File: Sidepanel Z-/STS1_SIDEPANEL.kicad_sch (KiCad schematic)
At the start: 7 parts, among them J1 Conn_01x18, J3 Conn_01x12

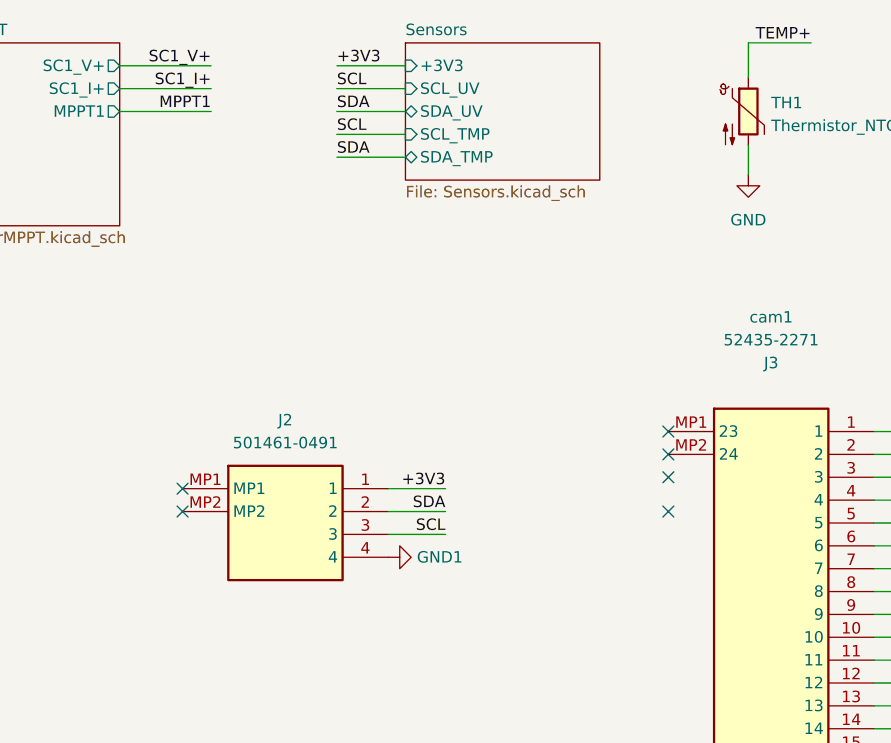
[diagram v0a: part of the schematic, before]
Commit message: replace ZF5S-*-01-T-WT and 2005280040 connectors with T1M-*-F-SH-L-FR connector
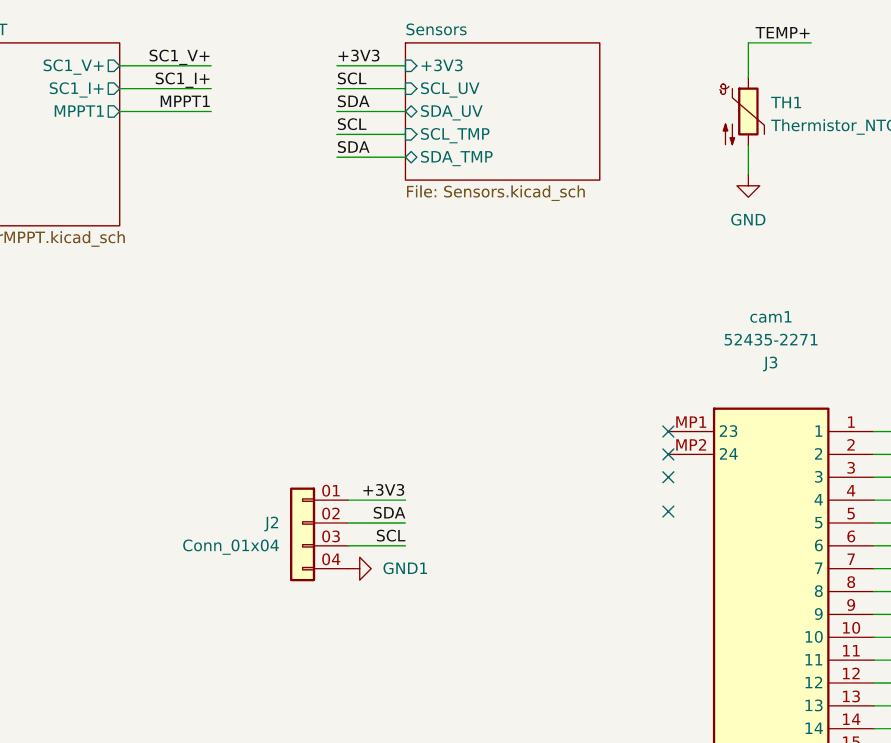
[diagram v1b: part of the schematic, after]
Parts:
- removed UV1: 501461-0491, STS_connector:200528-0040, symbol Connector:501461-0491
- added J2: Conn_01x04, STS_connector:SAMTEC_T1M-04-X-SH-L, symbol Connector_Generic:Conn_01x04
- J1: footprint STS_connector:SAMTEC_ZF5S-16-01-T-WT -> STS_connector:SAMTEC_T1M-16-F-SH-L
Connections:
- net +3V3: now also J2.01 (Pin_1)
- net GND1: now also J2.04 (Pin_4)
- net SCL: now also J2.03 (Pin_3)
- net SDA: now also J2.02 (Pin_2)
- no-connect marks 13 -> 11

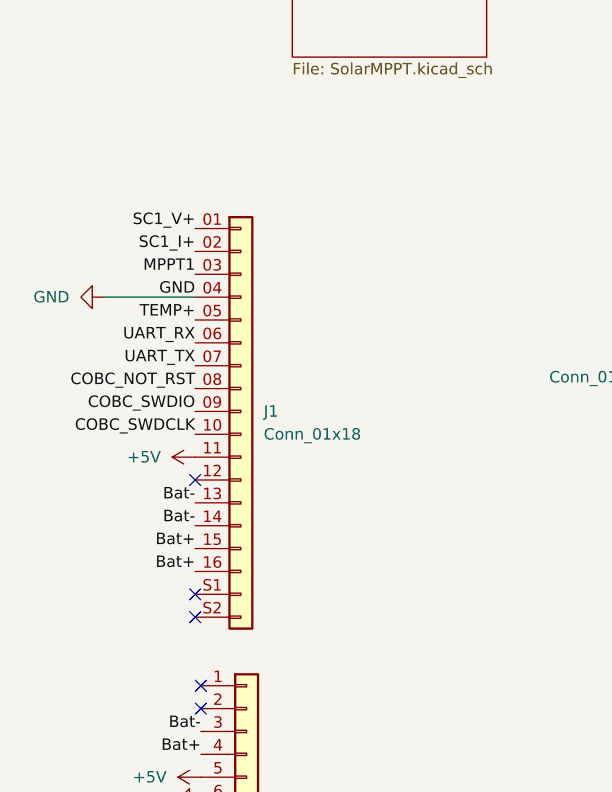
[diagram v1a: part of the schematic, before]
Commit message: mirror the pinout of the connector on the Z- panel, split output capacitor in two capacitors
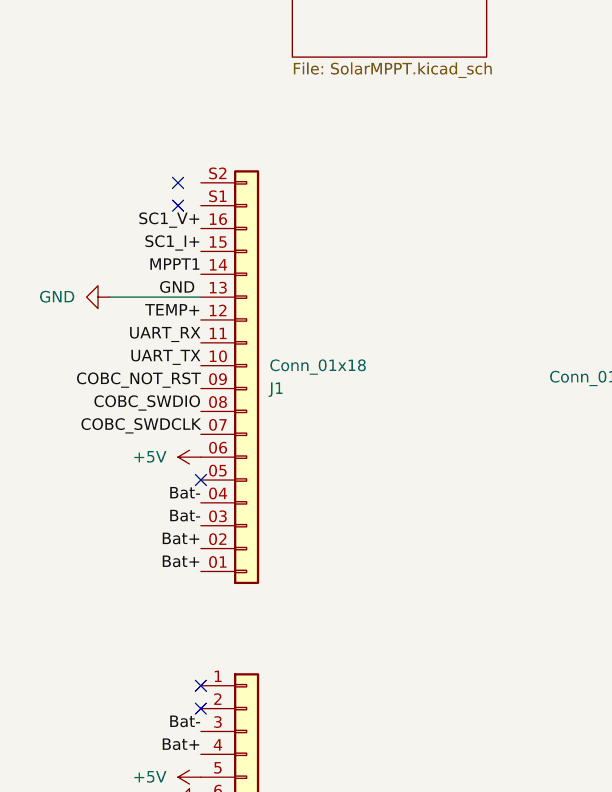
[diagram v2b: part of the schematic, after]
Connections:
- net +5V: now also J1.06 (Pin_6); no longer J1.11 (Pin_11)
- net Bat+: now also J1.01 (Pin_1), J1.02 (Pin_2); no longer J1.15 (Pin_15), J1.16 (Pin_16)
- net Bat-: now also J1.03 (Pin_3), J1.04 (Pin_4); no longer J1.13 (Pin_13), J1.14 (Pin_14)
- net COBC_NOT_RST: now also J1.09 (Pin_9); no longer J1.08 (Pin_8)
- net COBC_SWDCLK: now also J1.07 (Pin_7); no longer J1.10 (Pin_10)
- net COBC_SWDIO: now also J1.08 (Pin_8); no longer J1.09 (Pin_9)
- net GND: now also J1.13 (Pin_13); no longer J1.04 (Pin_4)
- net MPPT1: now also J1.14 (Pin_14); no longer J1.03 (Pin_3)
- net SC1_I+: now also J1.15 (Pin_15); no longer J1.02 (Pin_2)
- net SC1_V+: now also J1.16 (Pin_16); no longer J1.01 (Pin_1)
- net TEMP+: now also J1.12 (Pin_12); no longer J1.05 (Pin_5)
- net UART_RX: now also J1.11 (Pin_11); no longer J1.06 (Pin_6)
- net UART_TX: now also J1.10 (Pin_10); no longer J1.07 (Pin_7)
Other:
- moved on the sheet: J1
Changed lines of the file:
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@@
 	)
 	(no_connect
-		(at 40.005 93.98)
+		(at 40.64 93.98)
 	)
 	(no_connect
@@
 	)
 	(no_connect
-		(at 40.005 109.22)
+		(at 38.1 63.5)
 	)
 	(no_connect
@@
 	)
 	(no_connect
-		(at 40.005 106.68)
+		(at 38.1 60.96)
 	)
 	(wire
@@
 	(wire
 		(pts
-			(xy 29.845 73.66) (xy 40.005 73.66)
+			(xy 30.48 73.66) (xy 40.64 73.66)
 		)
 		(stroke
@@
 	)
 	(label "COBC_SWDIO"
-		(at 40.005 86.36 180)
+		(at 40.64 86.36 180)
 		(effects
 			(font
@@
 	)
 	(label "Bat+"
-		(at 40.005 104.14 180)
+		(at 40.64 104.14 180)
 		(effects
 			(font
@@
 	)
 	(label "TEMP+"
-		(at 40.005 76.2 180)
+		(at 40.64 76.2 180)
 		(effects
 			(font
@@
 	)
 	(label "UART_TX"
-		(at 40.005 81.28 180)
+		(at 40.64 81.28 180)
 		(effects
 			(font
@@
 	)
 	(label "UART_RX"
-		(at 40.005 78.74 180)
+		(at 40.64 78.74 180)
 		(effects
 			(font
@@
 	)
 	(label "COBC_SWDCLK"
-		(at 40.005 88.9 180)
+		(at 40.64 88.9 180)
 		(effects
 			(font
@@
 	)
 	(label "Bat-"
-		(at 40.005 99.06 180)
+		(at 40.64 99.06 180)
 		(effects
 			(font
@@
 	)
 	(label "Bat-"
-		(at 40.005 96.52 180)
+		(at 40.64 96.52 180)
 		(effects
 			(font
@@
 	)
 	(label "Bat+"
-		(at 40.005 101.6 180)
+		(at 40.64 101.6 180)
 		(effects
 			(font
@@
 	)
 	(label "SC1_V+"
-		(at 40.005 66.04 180)
+		(at 40.64 66.04 180)
 		(effects
 			(font
@@
 	)
 	(label "COBC_NOT_RST"
-		(at 40.005 83.82 180)
+		(at 40.64 83.82 180)
 		(effects
 			(font
@@
 	)
 	(label "SC1_I+"
-		(at 40.005 68.58 180)
+		(at 40.64 68.58 180)
 		(effects
 			(font
@@
 	)
 	(label "MPPT1"
-		(at 40.005 71.12 180)
+		(at 40.64 71.12 180)
 		(effects
 			(font
@@
 	(symbol
 		(lib_id "power:GND")
-		(at 29.845 73.66 270)
+		(at 30.48 73.66 270)
 		(unit 1)
 		(body_style 1)
@@
 		(fields_autoplaced yes)
 		(property "Reference" "#PWR0111"
-			(at 23.495 73.66 0)
+			(at 24.13 73.66 0)
 			(hide yes)
 			(show_name no)
@@
 		)
 		(property "Value" "GND"
-			(at 26.035 73.6599 90)
+			(at 26.67 73.6599 90)
 			(show_name no)
 			(do_not_autoplace no)
@@
 		)
 		(property "Footprint" ""
-			(at 29.845 73.66 0)
+			(at 30.48 73.66 0)
 			(hide yes)
 			(show_name no)
@@
 		)
 		(property "Datasheet" ""
-			(at 29.845 73.66 0)
+			(at 30.48 73.66 0)
 			(hide yes)
 			(show_name no)
@@
 		)
 		(property "Description" ""
-			(at 29.845 73.66 0)
+			(at 30.48 73.66 0)
 			(hide yes)
 			(show_name no)
@@
 	(symbol
 		(lib_id "power:+5V")
-		(at 40.005 91.44 90)
+		(at 40.64 91.44 90)
 		(unit 1)
 		(body_style 1)
@@
 		(fields_autoplaced yes)
 		(property "Reference" "#PWR08"
-			(at 43.815 91.44 0)
+			(at 44.45 91.44 0)
 			(hide yes)
 			(show_name no)
@@
 		)
 		(property "Value" "+5V"
-			(at 36.195 91.44 90)
+			(at 36.83 91.44 90)
 			(show_name no)
 			(do_not_autoplace no)
@@
 		)
 		(property "Footprint" ""
-			(at 40.005 91.44 0)
+			(at 40.64 91.44 0)
 			(hide yes)
 			(show_name no)
@@
 		)
 		(property "Datasheet" ""
-			(at 40.005 91.44 0)
+			(at 40.64 91.44 0)
 			(hide yes)
 			(show_name no)
@@
 		)
 		(property "Description" ""
-			(at 40.005 91.44 0)
+			(at 40.64 91.44 0)
 			(hide yes)
 			(show_name no)
@@
 	(symbol
 		(lib_id "Connector_Generic:Conn_01x18")
-		(at 45.085 86.36 0)
+		(at 45.72 83.82 0)
+		(mirror x)
 		(unit 1)
 		(body_style 1)
@@
 		(in_pos_files yes)
 		(dnp no)
-		(fields_autoplaced yes)
 		(property "Reference" "J1"
-			(at 47.625 86.36 0)
+			(at 48.26 83.82 0)
 			(show_name no)
 			(do_not_autoplace no)
@@
 		)
 		(property "Value" "Conn_01x18"
-			(at 47.625 88.9 0)
+			(at 48.26 81.28 0)
 			(show_name no)
 			(do_not_autoplace no)
@@
 		)
 		(property "Footprint" "STS_connector:SAMTEC_T1M-16-F-SH-L"
-			(at 45.085 86.36 0)
+			(at 45.72 83.82 0)
 			(hide yes)
 			(show_name no)
@@
 		)
 		(property "Datasheet" ""
-			(at 45.085 86.36 0)
+			(at 45.72 83.82 0)
 			(hide yes)
 			(show_name no)
@@
 		)
 		(property "Description" ""
-			(at 45.085 86.36 0)
-			(hide yes)
-			(show_name no)
+			(at 45.72 83.82 0)
+			(hide yes)
+			(show_name no)
